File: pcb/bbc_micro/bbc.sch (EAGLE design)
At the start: 24 parts, among them U2 LM2776

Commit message: updated BBC micro PCB
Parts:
- removed C7: (no value), adafruit:CPOL-USE2.5-6
- added C2, C9: 470uF, rcl:CPOL-USSMCD
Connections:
- net +5V: now also C2.+; no longer C7.+
- net GND: now also C2.-, C9.-; no longer C7.-
- net N$1: now also C9.+
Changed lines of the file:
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@@
 <part name="P+5" library="supply1" library_urn="urn:adsk.eagle:library:371" deviceset="+5V" device=""/>
 <part name="C6" library="clock" deviceset="CAP" device="0805" value="1uF"/>
-<part name="C7" library="adafruit" deviceset="CPOL-US" device="E2.5-6"/>
 <part name="C8" library="clock" deviceset="CAP" device="0805" value="100nF"/>
 <part name="GND4" library="supply1" library_urn="urn:adsk.eagle:library:371" deviceset="GND" device=""/>
@@
 <part name="GND5" library="supply1" library_urn="urn:adsk.eagle:library:371" deviceset="GND" device=""/>
 <part name="GND8" library="supply1" library_urn="urn:adsk.eagle:library:371" deviceset="GND" device=""/>
+<part name="C2" library="rcl" library_urn="urn:adsk.eagle:library:334" deviceset="CPOL-US" device="SMCD" package3d_urn="urn:adsk.eagle:package:25923/2" value="470uF"/>
+<part name="C9" library="rcl" library_urn="urn:adsk.eagle:library:334" deviceset="CPOL-US" device="SMCD" package3d_urn="urn:adsk.eagle:package:25923/2" value="470uF"/>
+<part name="GND9" library="supply1" library_urn="urn:adsk.eagle:library:371" deviceset="GND" device=""/>
 </parts>
 <sheets>
@@
 <attribute name="VALUE" x="155.956" y="177.419" size="1.778" layer="96" rot="R180"/>
 </instance>
-<instance part="C7" gate="G$1" x="167.64" y="175.26" smashed="yes">
-<attribute name="NAME" x="168.656" y="175.895" size="1.778" layer="95"/>
-<attribute name="VALUE" x="168.656" y="171.069" size="1.778" layer="96"/>
-</instance>
 <instance part="C8" gate="G$1" x="355.6" y="160.02" smashed="yes" rot="R180">
 <attribute name="NAME" x="354.076" y="157.099" size="1.778" layer="95" rot="R180"/>
@@
 <instance part="GND8" gate="1" x="317.5" y="152.4" smashed="yes">
 <attribute name="VALUE" x="314.96" y="149.86" size="1.778" layer="96"/>
+</instance>
+<instance part="C2" gate="G$1" x="167.64" y="175.26" smashed="yes">
+<attribute name="NAME" x="168.656" y="175.895" size="1.778" layer="95"/>
+<attribute name="VALUE" x="168.656" y="171.069" size="1.778" layer="96"/>
+</instance>
+<instance part="C9" gate="G$1" x="139.7" y="208.28" smashed="yes">
+<attribute name="NAME" x="140.716" y="208.915" size="1.778" layer="95"/>
+<attribute name="VALUE" x="140.716" y="204.089" size="1.778" layer="96"/>
+</instance>
+<instance part="GND9" gate="1" x="139.7" y="200.66" smashed="yes">
+<attribute name="VALUE" x="137.16" y="198.12" size="1.778" layer="96"/>
 </instance>
 </instances>
@@
 <wire x1="157.48" y1="167.64" x2="147.32" y2="167.64" width="0.1524" layer="91"/>
 <junction x="147.32" y="167.64"/>
-<pinref part="C7" gate="G$1" pin="-"/>
 <wire x1="157.48" y1="167.64" x2="167.64" y2="167.64" width="0.1524" layer="91"/>
+<junction x="157.48" y="167.64"/>
+<pinref part="C2" gate="G$1" pin="-"/>
 <wire x1="167.64" y1="167.64" x2="167.64" y2="170.18" width="0.1524" layer="91"/>
-<junction x="157.48" y="167.64"/>
 </segment>
 <segment>
@@
 <pinref part="C4" gate="G$1" pin="2"/>
 <pinref part="GND8" gate="1" pin="GND"/>
+</segment>
+<segment>
+<pinref part="C9" gate="G$1" pin="-"/>
+<pinref part="GND9" gate="1" pin="GND"/>
 </segment>
 </net>
@@
 <wire x1="157.48" y1="180.34" x2="157.48" y2="177.8" width="0.1524" layer="91"/>
 <junction x="147.32" y="180.34"/>
-<pinref part="C7" gate="G$1" pin="+"/>
 <wire x1="157.48" y1="180.34" x2="167.64" y2="180.34" width="0.1524" layer="91"/>
+<junction x="157.48" y="180.34"/>
+<pinref part="C2" gate="G$1" pin="+"/>
 <wire x1="167.64" y1="180.34" x2="167.64" y2="177.8" width="0.1524" layer="91"/>
-<junction x="157.48" y="180.34"/>
 </segment>
 <segment>
@@
 <wire x1="203.2" y1="200.66" x2="215.9" y2="200.66" width="0.1524" layer="91"/>
 <junction x="215.9" y="200.66"/>
-<wire x1="132.08" y1="210.82" x2="165.1" y2="210.82" width="0.1524" layer="91"/>
+<wire x1="132.08" y1="210.82" x2="139.7" y2="210.82" width="0.1524" layer="91"/>
 <junction x="165.1" y="210.82"/>
 <pinref part="J4" gate="J1" pin="VBUS"/>
+<wire x1="139.7" y1="210.82" x2="165.1" y2="210.82" width="0.1524" layer="91"/>
 <wire x1="104.14" y1="215.9" x2="132.08" y2="215.9" width="0.1524" layer="91"/>
 <wire x1="132.08" y1="215.9" x2="132.08" y2="210.82" width="0.1524" layer="91"/>
+<pinref part="C9" gate="G$1" pin="+"/>
+<junction x="139.7" y="210.82"/>
 </segment>
 </net>
@@
 packages will not be understood (or retained) with this version.
 </note>
+<note version="8.4" severity="warning">
+Since Version 8.4, EAGLE supports properties for SPICE simulation.
+Probes in schematics and SPICE mapping objects found in parts and library devices
+will not be understood with this version. Update EAGLE to the latest version
+for full support of SPICE simulation.
+</note>
 </compatibility>

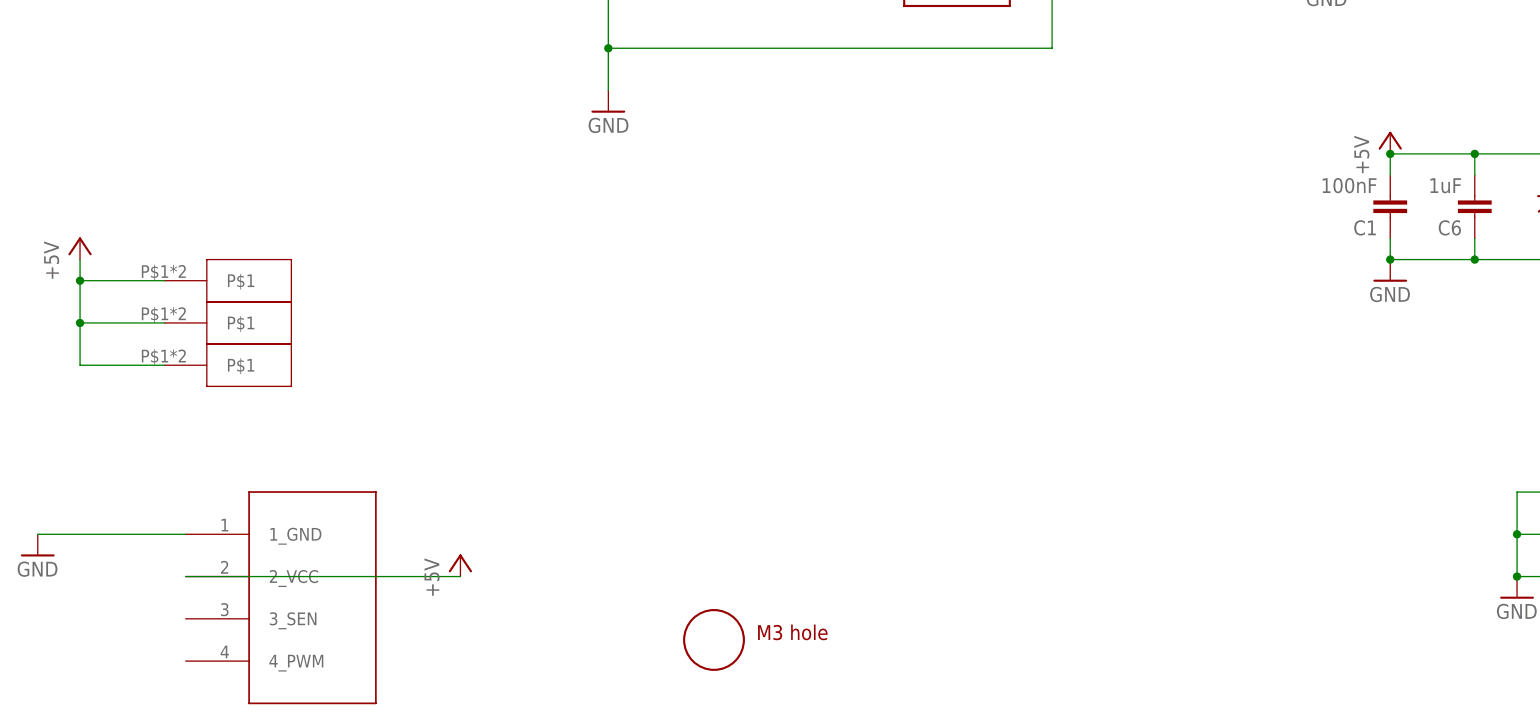
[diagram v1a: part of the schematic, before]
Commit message: updated fan header
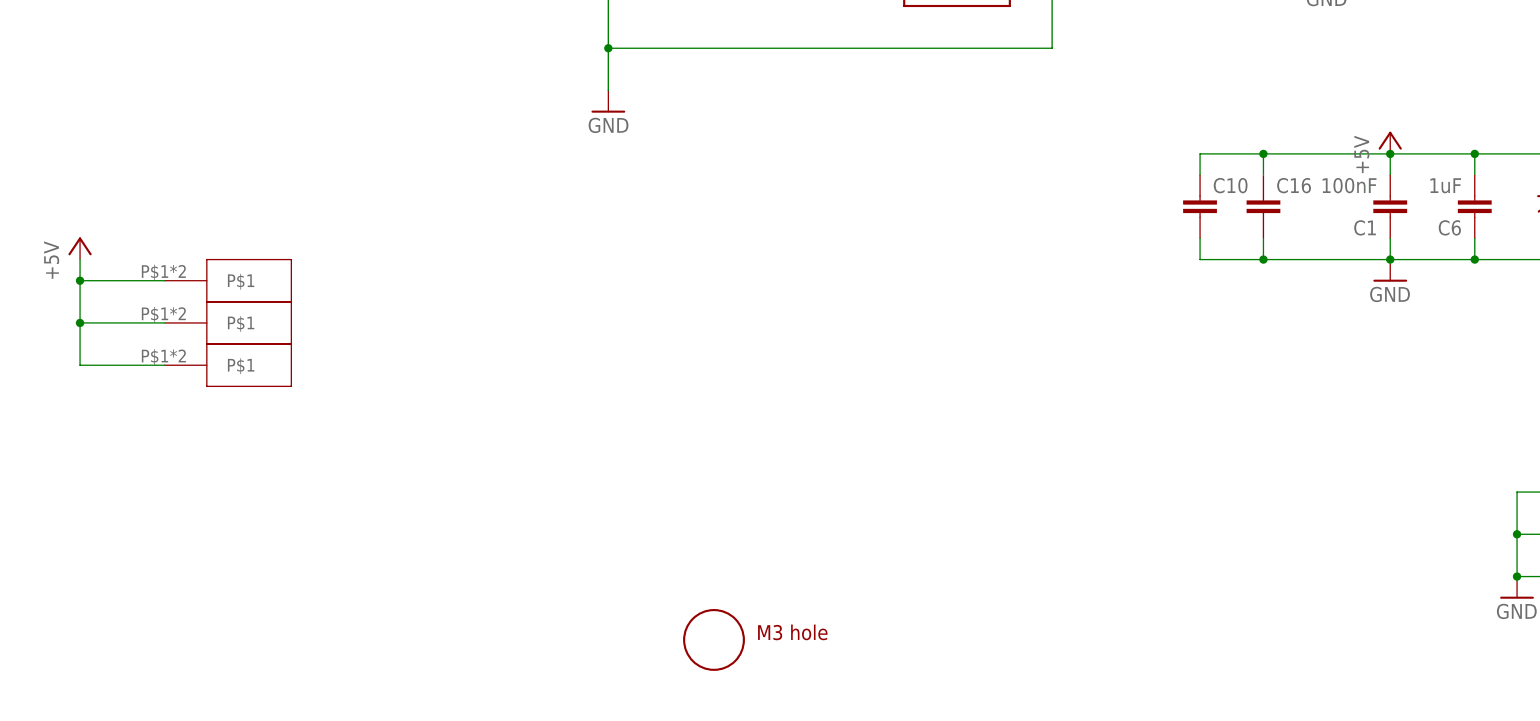
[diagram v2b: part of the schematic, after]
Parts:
- removed JP3: (no value), appleii:4PIN_FAN
- added C10, C16: (no value), capacitor-wima:C5/2.5
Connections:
- net +5V: now also C10.1, C16.1; no longer JP3.2_VCC
- net GND: now also C10.2, C16.2; no longer JP3.1_GND
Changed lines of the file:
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@@
 <?xml version="1.0" encoding="utf-8"?>
 <!DOCTYPE eagle SYSTEM "eagle.dtd">
-<eagle version="9.6.1">
+<eagle version="9.6.2">
 <drawing>
 <settings>
@@
 <parts>
 <part name="JP1" library="pinhead" library_urn="urn:adsk.eagle:library:325" deviceset="PINHD-1X2" device="" package3d_urn="urn:adsk.eagle:package:22435/2"/>
-<part name="GND7" library="supply1" library_urn="urn:adsk.eagle:library:371" deviceset="GND" device=""/>
 <part name="U$4" library="a" deviceset="M3_MOUNTING_HOLE" device=""/>
 <part name="U$3" library="atx4vc" deviceset="ROCK_SW" device=""/>
-<part name="JP3" library="appleii" deviceset="4PIN_FAN" device=""/>
 <part name="U$6" library="blade" deviceset="BLADE28" device=""/>
 <part name="U$7" library="blade" deviceset="BLADE28" device=""/>
@@
 <part name="P+4" library="supply1" library_urn="urn:adsk.eagle:library:371" deviceset="+5V" device=""/>
 <part name="GND3" library="supply1" library_urn="urn:adsk.eagle:library:371" deviceset="GND" device=""/>
-<part name="P+5" library="supply1" library_urn="urn:adsk.eagle:library:371" deviceset="+5V" device=""/>
 <part name="C6" library="clock" deviceset="CAP" device="0805" value="1uF"/>
 <part name="C8" library="clock" deviceset="CAP" device="0805" value="100nF"/>
@@
 <part name="C9" library="rcl" library_urn="urn:adsk.eagle:library:334" deviceset="CPOL-US" device="SMCD" package3d_urn="urn:adsk.eagle:package:25923/2" value="470uF"/>
 <part name="GND9" library="supply1" library_urn="urn:adsk.eagle:library:371" deviceset="GND" device=""/>
+<part name="C10" library="capacitor-wima" library_urn="urn:adsk.eagle:library:116" deviceset="C" device="5/2.5" package3d_urn="urn:adsk.eagle:package:5426/1"/>
+<part name="C16" library="capacitor-wima" library_urn="urn:adsk.eagle:library:116" deviceset="C" device="5/2.5" package3d_urn="urn:adsk.eagle:package:5426/1"/>
 </parts>
 <sheets>
@@
 <attribute name="VALUE" x="161.29" y="205.74" size="1.778" layer="96"/>
 </instance>
-<instance part="GND7" gate="1" x="-15.24" y="132.08" smashed="yes">
-<attribute name="VALUE" x="-17.78" y="129.54" size="1.778" layer="96"/>
-</instance>
 <instance part="U$4" gate="G$1" x="66.04" y="121.92" smashed="yes"/>
 <instance part="U$3" gate="G$1" x="220.98" y="210.82" smashed="yes" rot="R90"/>
-<instance part="JP3" gate="A" x="15.24" y="127" smashed="yes"/>
 <instance part="U$6" gate="G$1" x="10.16" y="160.02" smashed="yes"/>
 <instance part="U$7" gate="G$1" x="10.16" y="154.94" smashed="yes"/>
@@
 <attribute name="VALUE" x="144.78" y="162.56" size="1.778" layer="96"/>
 </instance>
-<instance part="P+5" gate="1" x="35.56" y="132.08" smashed="yes">
-<attribute name="VALUE" x="33.02" y="127" size="1.778" layer="96" rot="R90"/>
-</instance>
 <instance part="C6" gate="G$1" x="157.48" y="175.26" smashed="yes" rot="R180">
 <attribute name="NAME" x="155.956" y="172.339" size="1.778" layer="95" rot="R180"/>
@@
 <instance part="GND9" gate="1" x="139.7" y="200.66" smashed="yes">
 <attribute name="VALUE" x="137.16" y="198.12" size="1.778" layer="96"/>
+</instance>
+<instance part="C10" gate="G$1" x="124.46" y="175.26" smashed="yes">
+<attribute name="NAME" x="125.984" y="175.641" size="1.778" layer="95"/>
+<attribute name="VALUE" x="125.984" y="170.561" size="1.778" layer="96"/>
+</instance>
+<instance part="C16" gate="G$1" x="132.08" y="175.26" smashed="yes">
+<attribute name="NAME" x="133.604" y="175.641" size="1.778" layer="95"/>
+<attribute name="VALUE" x="133.604" y="170.561" size="1.778" layer="96"/>
 </instance>
 </instances>
@@
 <nets>
 <net name="GND" class="0">
-<segment>
-<pinref part="JP3" gate="A" pin="1_GND"/>
-<pinref part="GND7" gate="1" pin="GND"/>
-<wire x1="2.54" y1="134.62" x2="-15.24" y2="134.62" width="0.1524" layer="91"/>
-</segment>
 <segment>
 <pinref part="U$9" gate="G$1" pin="P$1"/>
@@
 <pinref part="C2" gate="G$1" pin="-"/>
 <wire x1="167.64" y1="167.64" x2="167.64" y2="170.18" width="0.1524" layer="91"/>
+<pinref part="C10" gate="G$1" pin="2"/>
+<wire x1="124.46" y1="170.18" x2="124.46" y2="167.64" width="0.1524" layer="91"/>
+<wire x1="124.46" y1="167.64" x2="132.08" y2="167.64" width="0.1524" layer="91"/>
+<pinref part="C16" gate="G$1" pin="2"/>
+<wire x1="132.08" y1="167.64" x2="147.32" y2="167.64" width="0.1524" layer="91"/>
+<wire x1="132.08" y1="170.18" x2="132.08" y2="167.64" width="0.1524" layer="91"/>
+<junction x="132.08" y="167.64"/>
 </segment>
 <segment>
@@
 <pinref part="C2" gate="G$1" pin="+"/>
 <wire x1="167.64" y1="180.34" x2="167.64" y2="177.8" width="0.1524" layer="91"/>
-</segment>
-<segment>
-<pinref part="P+5" gate="1" pin="+5V"/>
-<pinref part="JP3" gate="A" pin="2_VCC"/>
-<wire x1="35.56" y1="129.54" x2="2.54" y2="129.54" width="0.1524" layer="91"/>
-</segment>
-<segment>
+<pinref part="C10" gate="G$1" pin="1"/>
+<wire x1="147.32" y1="180.34" x2="132.08" y2="180.34" width="0.1524" layer="91"/>
+<wire x1="132.08" y1="180.34" x2="124.46" y2="180.34" width="0.1524" layer="91"/>
+<wire x1="124.46" y1="180.34" x2="124.46" y2="177.8" width="0.1524" layer="91"/>
+<pinref part="C16" gate="G$1" pin="1"/>
+<wire x1="132.08" y1="177.8" x2="132.08" y2="180.34" width="0.1524" layer="91"/>
+<junction x="132.08" y="180.34"/>
+</segment>
+<segment>
